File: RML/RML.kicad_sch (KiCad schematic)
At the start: 15 parts, among them J1 Conn_01x02, J2 Conn_01x02, U1 LR8K4-G, U3 SFH617A-1, X1 OCXO-14

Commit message: RML Fixes
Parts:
- removed D2, D3: LED, symbol Device:LED
- removed R3, R4, R5: R_US, symbol Device:R_US
- removed X1: OCXO-14, Oscillator:Oscillator_DIP-14, symbol Oscillator:OCXO-14
- added C101: ~, symbol Device:C_Polarized_Small_US
- added D101: D_TVS, symbol Device:D_TVS
- added R101: 220R, symbol Device:R_US
- added U101: LMC555xM, Package_SO:SOIC-8_3.9x4.9mm_P1.27mm, symbol Timer:LMC555xM
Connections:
- net GND: now also C101.2, D101.1 (A1), R101.2; no longer U3.2
- net at C1.1, D1.2 (A), R2.1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: now also U3.1
- net at D1.1 (K), J1.2 (Pin_2), U1.1 (IN): now also C101.1
- net at J2.1 (0-352.8V), U3.4: now also D101.2 (A2)
- new net: R101.1, U3.2
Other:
- note added: "Make Forward Current = 10mA"
- note added: "Vf = 1.35 typical"
- note added: "~16.5mA If"
- moved on the sheet: J2, R6

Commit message: Edits to RML
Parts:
- added C102: 10u, symbol Device:C_Polarized_Small_US
- C1, C101: value ~ -> 1u
- R1: value R_US -> 18.2k
- R2: value R_US -> 6.04k
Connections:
- net GND: now also C102.2
- net at C1.1, D1.2 (A), R2.1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: now also C102.1
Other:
- note added: "1%"
- note added: "Iout = 20mA"
- moved on the sheet: C1, C101, J1, R1, R2, U1

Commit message: RML Connectors
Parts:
- removed J1, J2: Conn_01x02, symbol Connector_Generic:Conn_01x02
- removed R6: 1k, symbol Device:R_US
- added Q101: PMOS, symbol Simulation_SPICE:PMOS
- added R102: 10k, symbol Device:R_US
- added U102, U103: 641964-1, 641964-1_TYC, symbol CONNECTOR:641964-1
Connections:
- net GND: now also U3.3, U102.2, U103.2
- net at D101.2 (A2): now also Q101.1 (D), U102.1; no longer U3.4
- net at C101.1, D1.1 (K), U1.1 (IN): now also U103.1
- new net: Q101.2 (G), R102.2, U3.4
- new net +12V: Q101.3 (S), R102.1
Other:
- note added: "(12.8 V - 0.243 A) * 2"
- note added: "0 - 352.8 V"
- note added: "POWER MOSFET"
- moved on the sheet: D101, U101

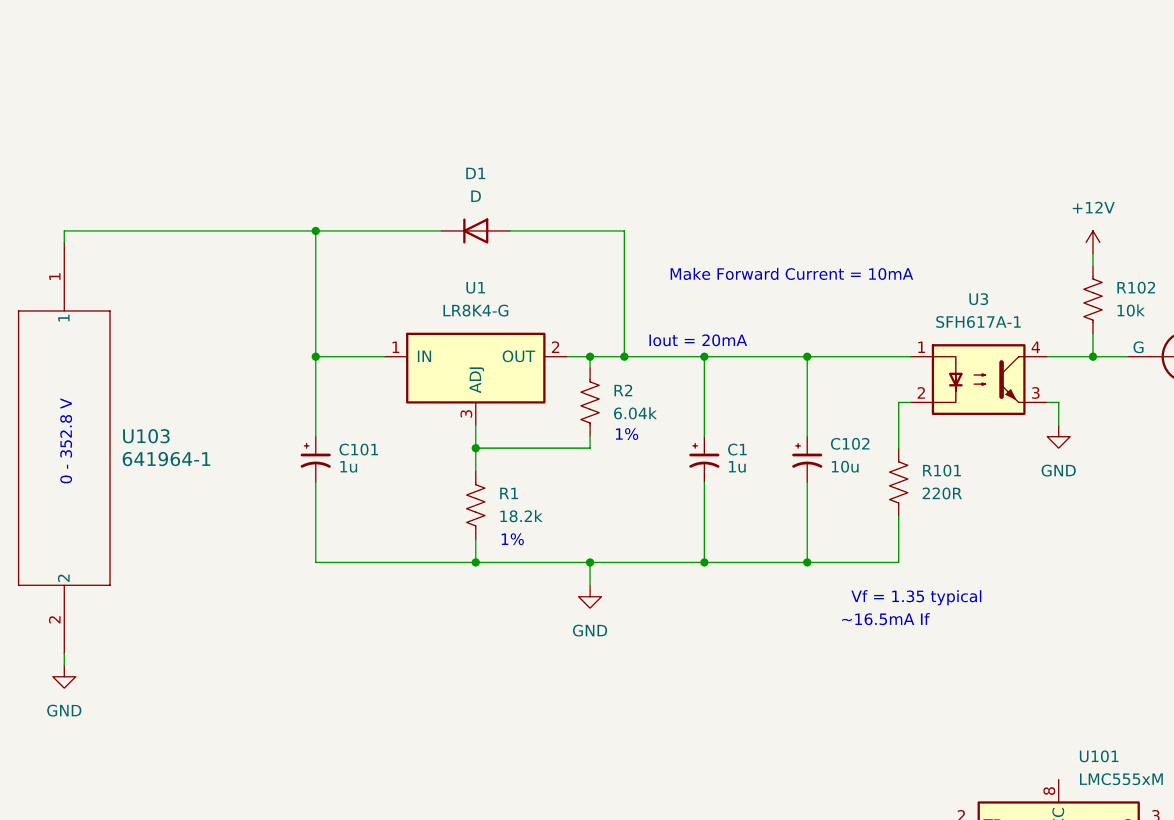
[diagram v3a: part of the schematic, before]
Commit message: Added series resistor to RML
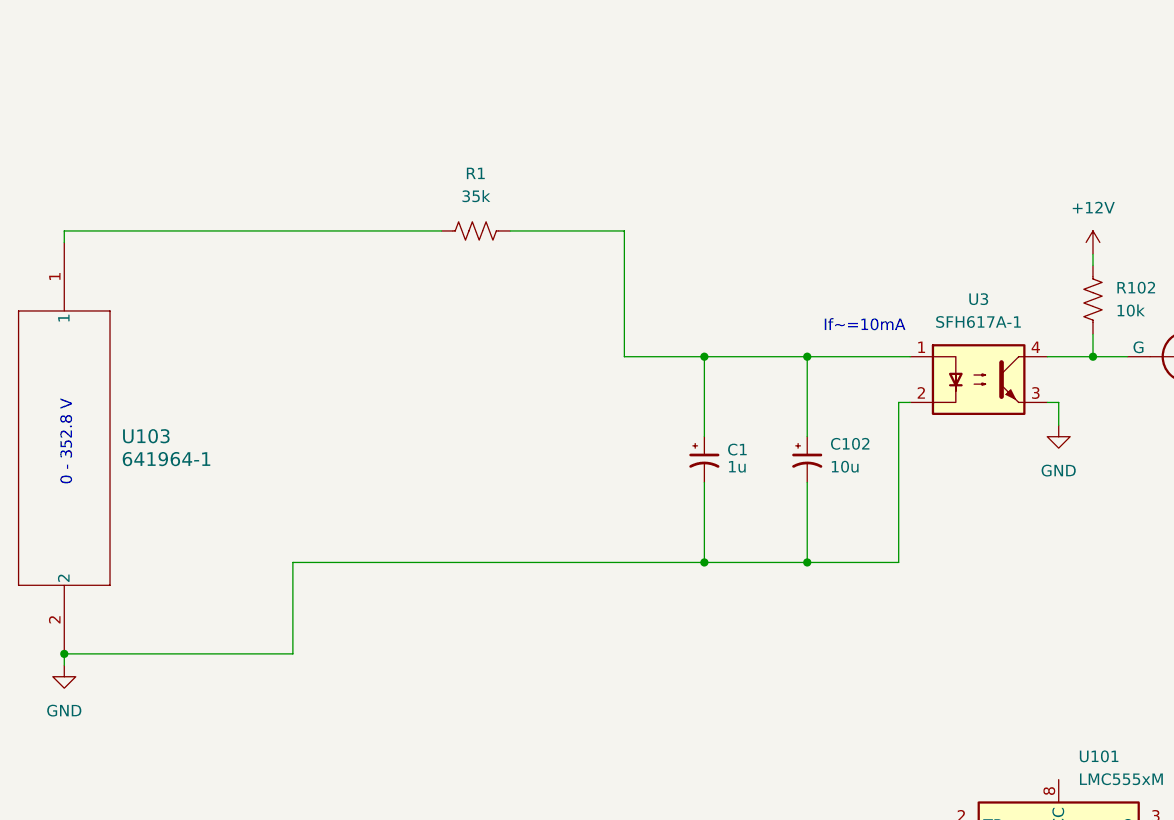
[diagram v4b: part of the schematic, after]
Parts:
- removed C101: 1u, symbol Device:C_Polarized_Small_US
- removed D1: D, symbol Device:D
- removed R101: 220R, symbol Device:R_US
- removed R2: 6.04k, symbol Device:R_US
- removed U1: LR8K4-G, Package_TO_SOT_SMD:TO-252-2, symbol Regulator_Linear:LR8K4-G
- R1: value 18.2k -> 35k
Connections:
- net GND: now also U3.2; no longer R1.2
- net at C1.1, C102.1, U3.1: now also R1.2
- net at R1.1: now also U103.1
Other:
- note added: "If~=10mA"
- note removed: "1%"
- note removed: "Iout = 20mA"
- note removed: "Make Forward Current = 10mA"
- note removed: "Vf = 1.35 typical"
- note removed: "~16.5mA If"

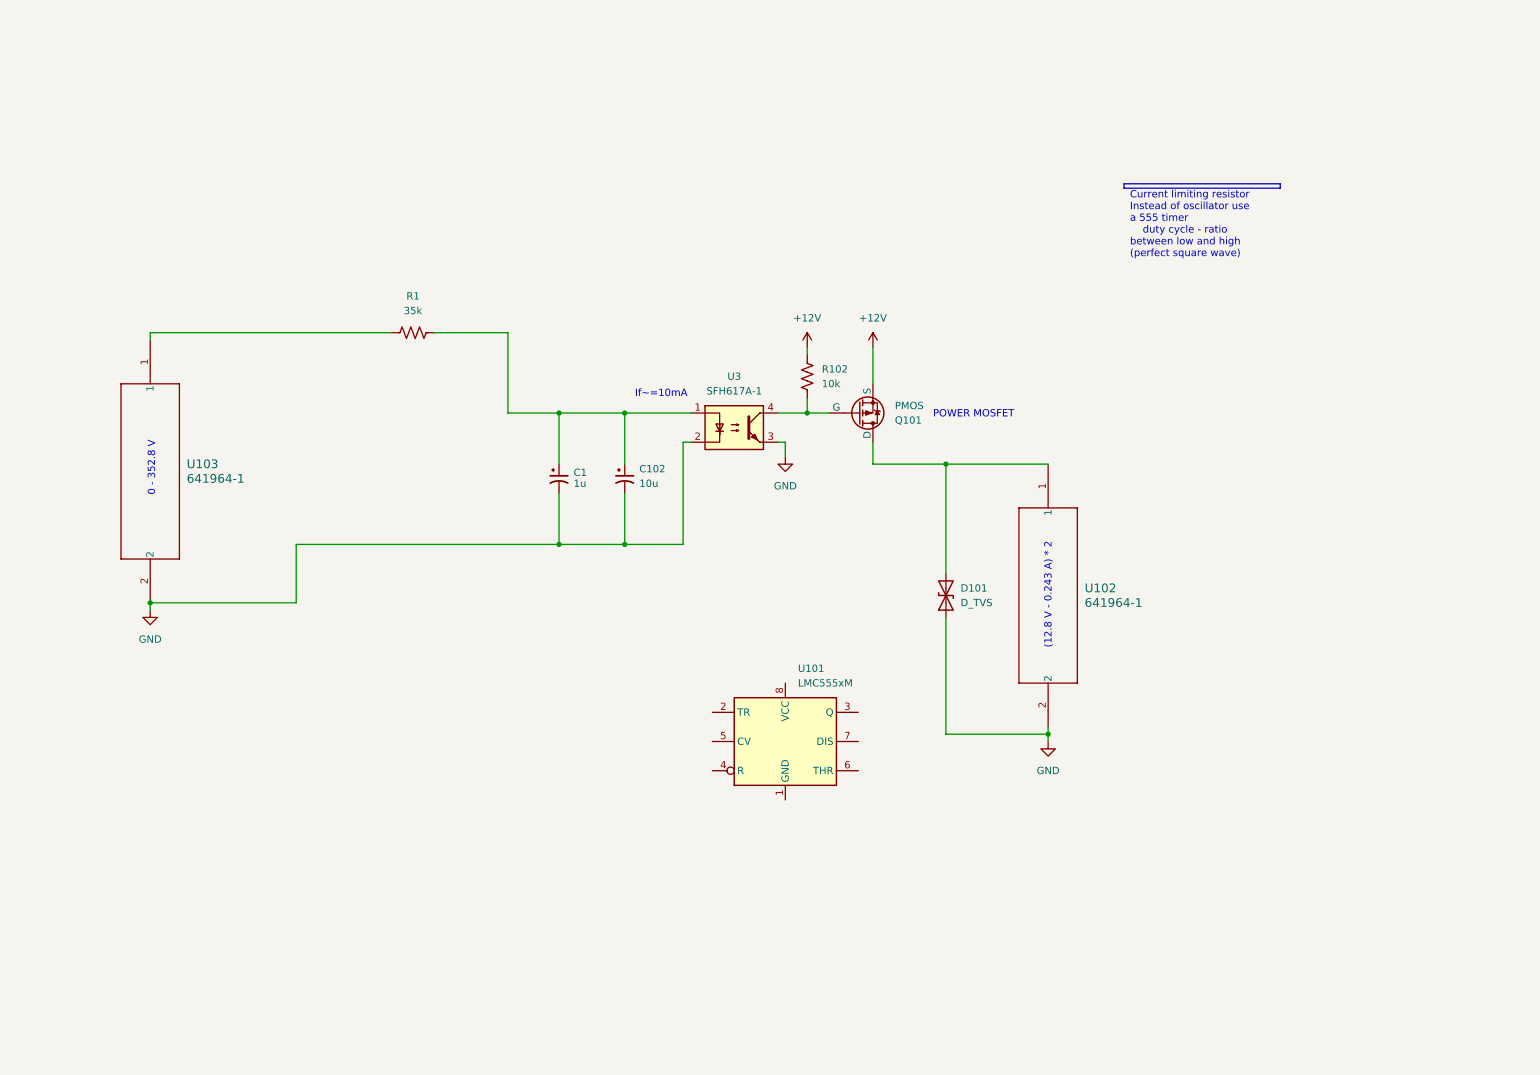
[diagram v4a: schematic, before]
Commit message: RML changes
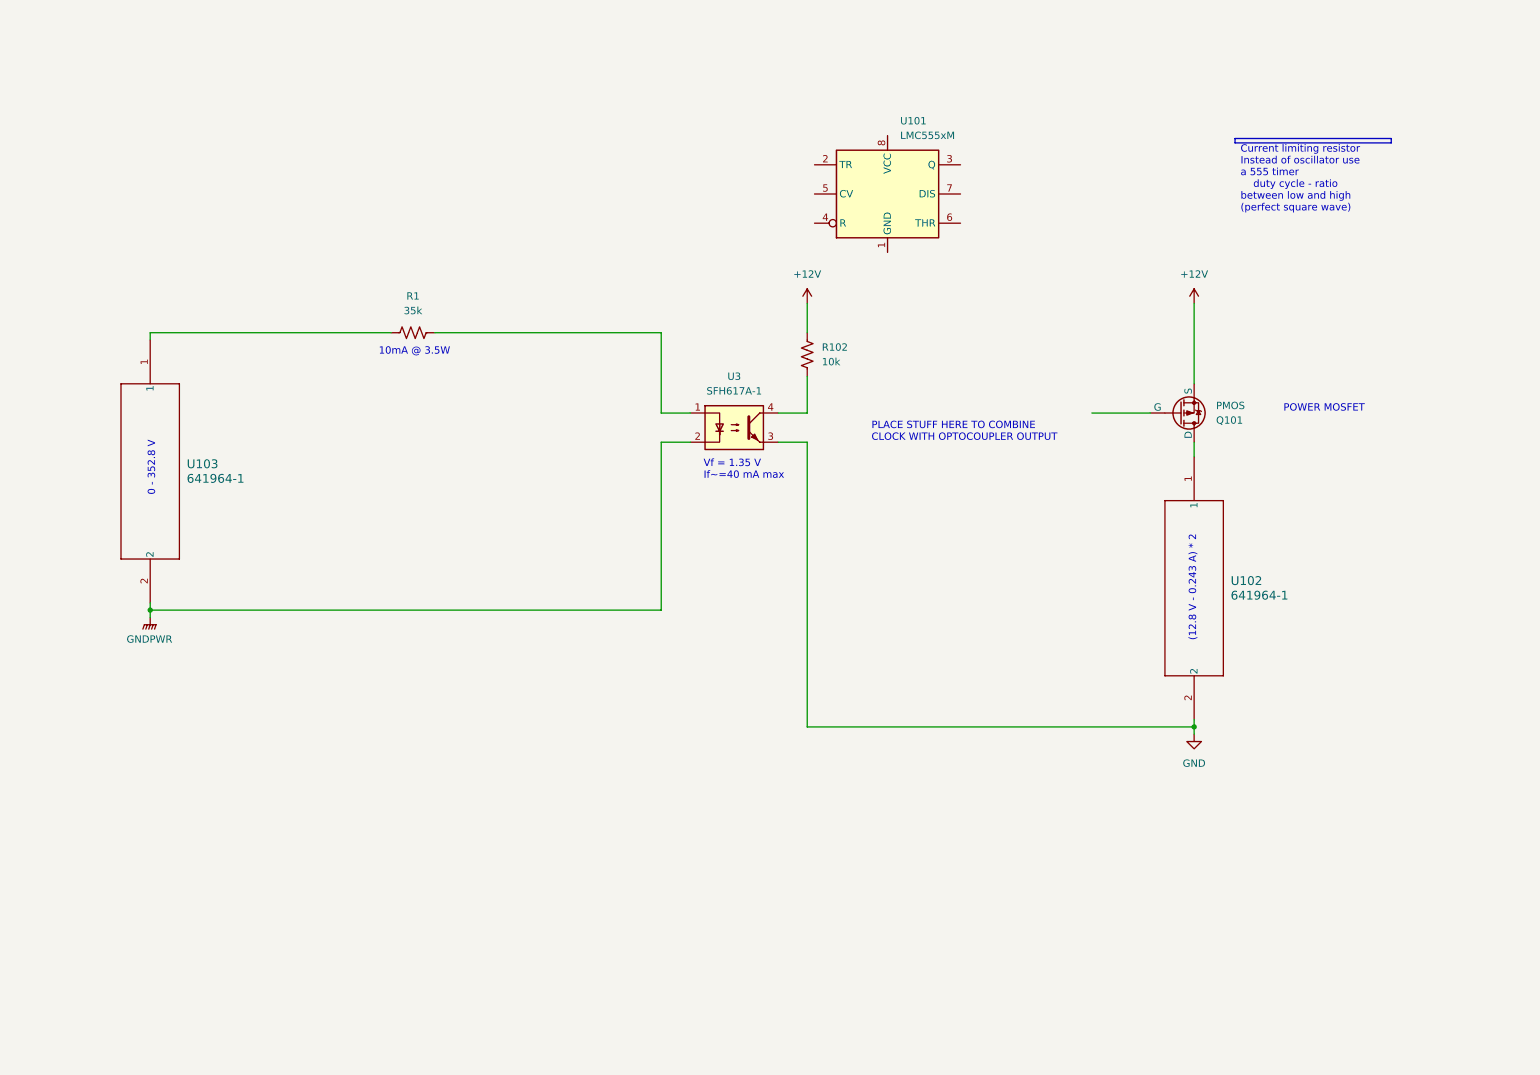
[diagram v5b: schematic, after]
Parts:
- removed C1: 1u, symbol Device:C_Polarized_Small_US
- removed C102: 10u, symbol Device:C_Polarized_Small_US
- removed D101: D_TVS, symbol Device:D_TVS
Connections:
- net GND: no longer U103.2, U3.2
- net at R102.2, U3.4: no longer Q101.2 (G)
- new net GNDPWR: U103.2, U3.2
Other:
- note added: "10mA @ 3.5W"
- note added: "PLACE STUFF HERE TO COMBINE CLOCK WITH OPTOCOUPLER OUTPUT"
- note added: "Vf = 1.35 V If~=40 mA max"
- note removed: "If~=10mA"
- moved on the sheet: Q101, R102, U101, U102

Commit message: RML Notes
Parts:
- added C101: 1u, symbol Device:C_Polarized_US
- added C102: 0.1u, Capacitor_SMD:C_0402_1005Metric, symbol Device:C
- added C103: .01u, Capacitor_SMD:C_0402_1005Metric, symbol Device:C
- added C105: C, Capacitor_SMD:C_0402_1005Metric, symbol Device:C
- added R105: R_US, symbol Device:R_US
- added R106: 100k, symbol Device:R_US
- added U104: LM555xM, Package_SO:SOIC-8_3.9x4.9mm_P1.27mm, symbol Timer:LM555xM
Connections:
- net GND: now also C101.2, C102.2, C103.2, C105.1, U104.1 (GND)
- new net: C101.1, C102.1, R106.2, U104.4 (R), U104.8 (VCC)
- new net: C103.1, U104.5 (CV)
- new net CLOCK: R105.1, U104.3 (Q)
- new net THRESH: C105.2, R105.2, R106.1, U104.2 (TR), U104.6 (THR)
- no-connect marks 0 -> 1
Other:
- moved on the sheet: U101

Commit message: RML Notes
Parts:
- removed Q101: PMOS, symbol Simulation_SPICE:PMOS
- removed U101: LMC555xM, Package_SO:SOIC-8_3.9x4.9mm_P1.27mm, symbol Timer:LMC555xM
- added C1: 0.33uF, symbol Device:C
- added C2: 0.01uF, symbol Device:C
- added Q1: NMOS, symbol Simulation_SPICE:NMOS
- added R2: 100k, symbol Device:R_US
- added U1: 74AHC1G02, symbol 74xGxx:74AHC1G02
- added U2: LM7805_TO220, Package_TO_SOT_THT:TO-220-3_Vertical, symbol Regulator_Linear:LM7805_TO220
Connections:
- net +12V: now also C1.1, Q1.3 (S), U2.1 (VI)
- net CLOCK: now also U1.2
- net GND: now also C1.2, C2.2, R2.2, U1.3 (GND), U2.2 (GND)
- net at U102.1: now also Q1.1 (D)
- net at R102.2, U3.4: now also U1.1
- new net: C2.1, U1.5 (VCC), U2.3 (VO)
- new net: Q1.2 (G), R2.1, U1.4
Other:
- note added: "555 Timer"
- note removed: "PLACE STUFF HERE TO COMBINE CLOCK WITH OPTOCOUPLER OUTPUT"
- moved on the sheet: C101, C102, C103, C105, R105, R106, U102, U104

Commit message: Fault Latch Overhaul
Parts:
- removed Q1: NMOS, symbol Simulation_SPICE:NMOS
- added Q?: NMOS, symbol Simulation_SPICE:NMOS
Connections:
- net +12V: now also Q?.1 (D)
- net GND: now also R2.1; no longer R2.2
- net at U1.4: now also R2.2, Q?.2 (G); no longer R2.1
- net at U102.1: now also Q?.3 (S)
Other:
- moved on the sheet: R2
